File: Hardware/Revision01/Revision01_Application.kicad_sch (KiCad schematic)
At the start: 43 parts, among them J2 StrainConn, J3 StrainConn, J4 StrainConn, J5 StrainConn, J6 StrainConn, J7 StrainConn, J8 StrainConn, J9 StrainConn, Q3 NMOS, Q4 PMOS, Q6 PMOS, U11 LP5813BDRRR, U2 MRF89XAM9AT-I/RM, U4 ICM-45605, U6 INA317xxDGK

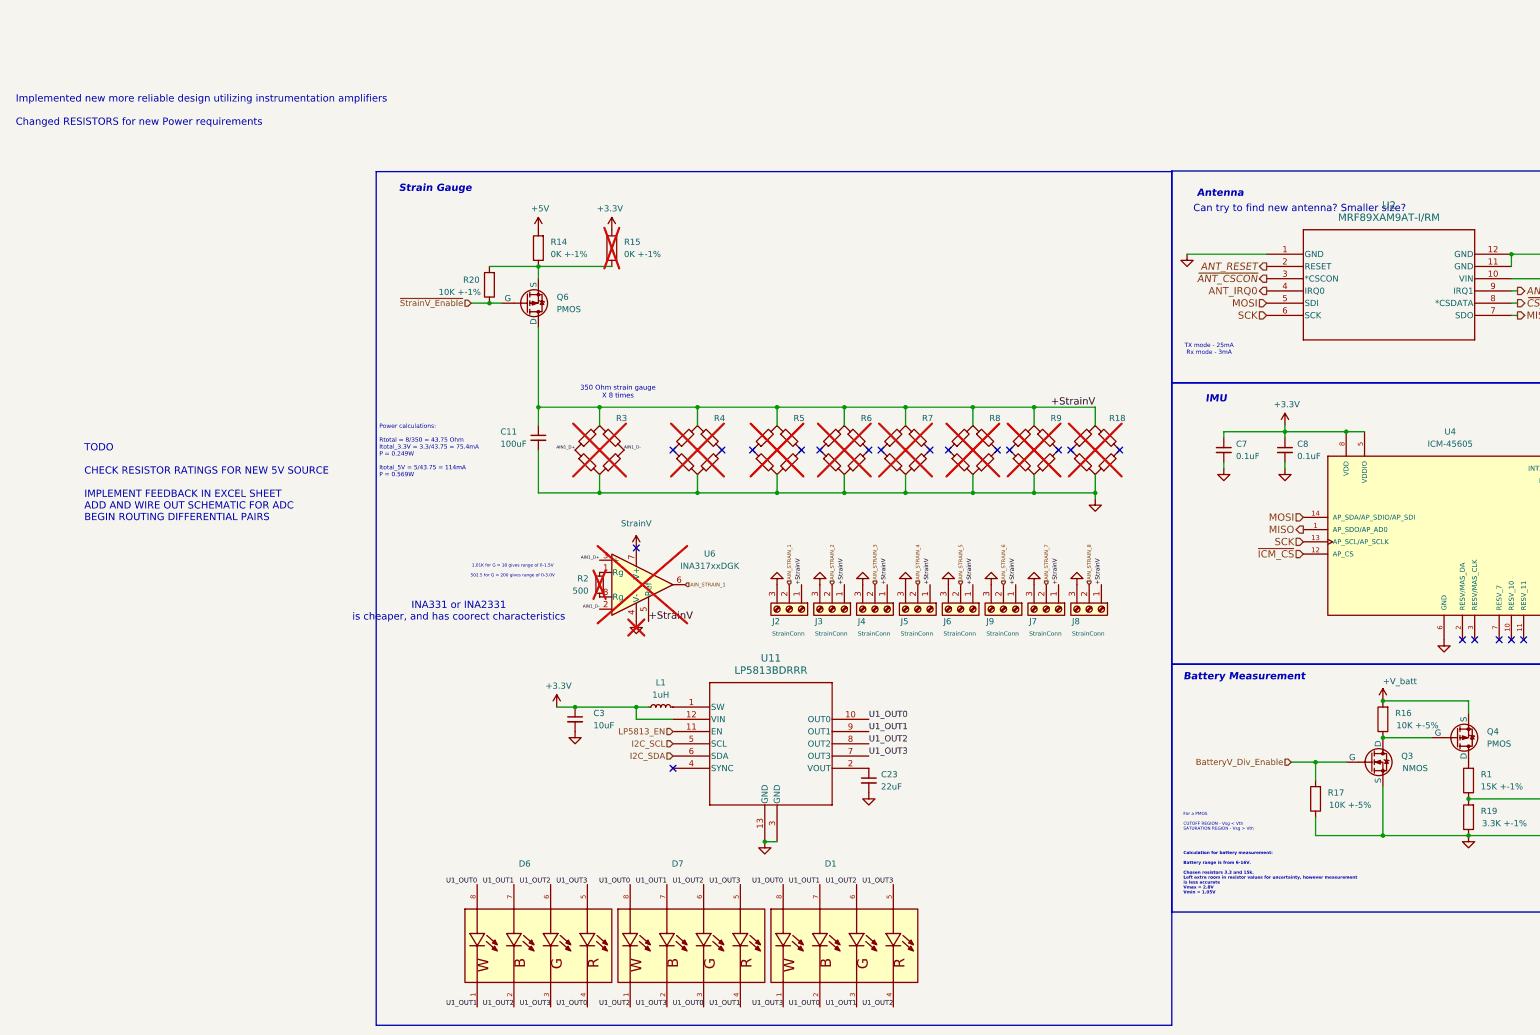
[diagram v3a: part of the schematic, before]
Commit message: Finished up small things(on schematic layout)
-Connector pins switched such that GND is pin 1
-used KICAD feature to indicate ACTIVE LOW
-polyFuse added to each StrainGauge
-Added Grounded Mounting holes connects to external GND(outside of PCB)
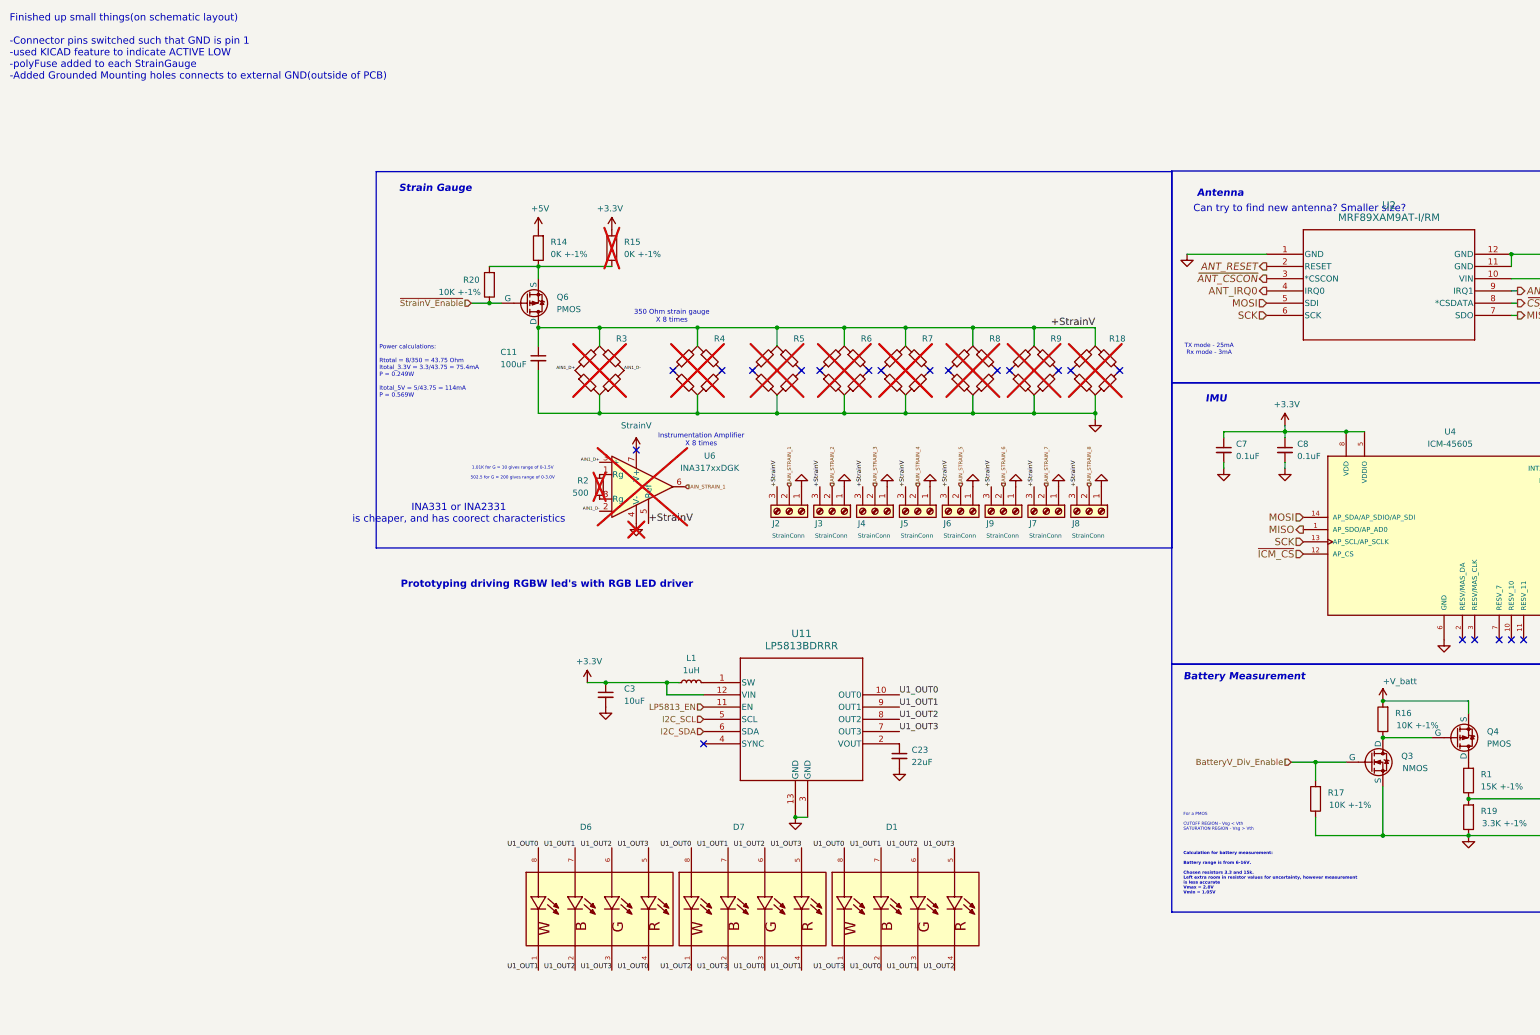
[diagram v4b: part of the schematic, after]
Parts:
- R16, R17: value 10K +-5% -> 10K +-1%
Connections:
- net +StrainV: now also J2.3 (Pin_3), J3.3 (Pin_3), J4.3 (Pin_3), J5.3 (Pin_3), J6.3 (Pin_3), J7.3 (Pin_3), J8.3 (Pin_3), J9.3 (Pin_3); no longer J2.1 (Pin_1), J3.1 (Pin_1), J4.1 (Pin_1), J5.1 (Pin_1), J6.1 (Pin_1), J7.1 (Pin_1), J8.1 (Pin_1), J9.1 (Pin_1)
- net GND: now also J2.1 (Pin_1), J3.1 (Pin_1), J4.1 (Pin_1), J5.1 (Pin_1), J6.1 (Pin_1), J7.1 (Pin_1), J8.1 (Pin_1), J9.1 (Pin_1); no longer J2.3 (Pin_3), J3.3 (Pin_3), J4.3 (Pin_3), J5.3 (Pin_3), J6.3 (Pin_3), J7.3 (Pin_3), J8.3 (Pin_3), J9.3 (Pin_3)
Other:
- note added: "Finished up small things(on schematic layout) -Connector pins switched such that GND is pin 1 -used KICAD feature to indicate ACTIVE LOW -polyFuse added to each StrainGauge -Added Grounded Mounting holes connects to external GND(outside of PCB)"
- note added: "Instrumentation Amplifier X 8 times"
- note added: "Prototyping driving RGBW led's with RGB LED driver"
- note removed: "Implemented new more reliable design utilizing instrumentation amplifiers Changed RESISTORS for new Power requirements"
- note removed: "TODO CHECK RESISTOR RATINGS FOR NEW 5V SOURCE IMPLEMENT FEEDBACK IN EXCEL SHEET ADD AND WIRE OUT SCHEMATIC FOR ADC BEGIN ROUTING DIFFERENTIAL PAIRS"
- moved on the sheet: C11, C23, C3, D1, D6, D7, J2, J3, J4, J5, J6, J7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

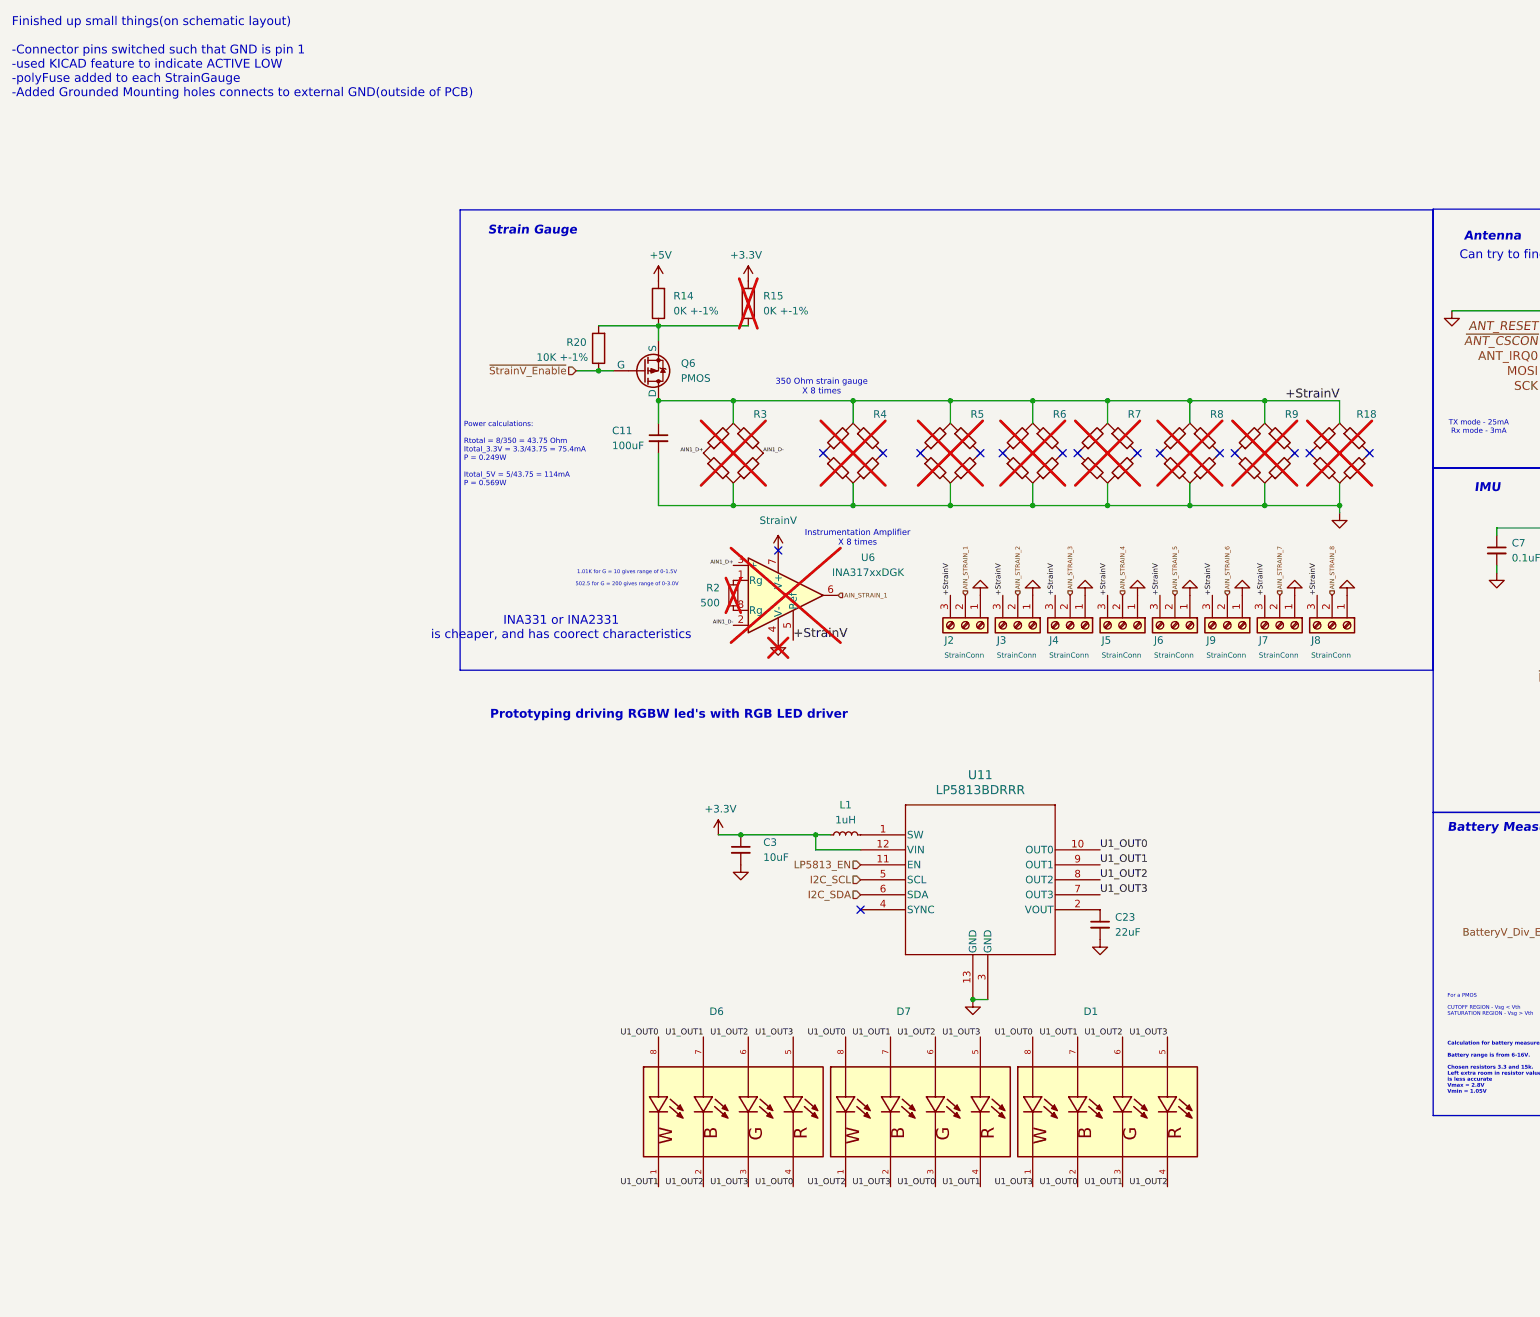
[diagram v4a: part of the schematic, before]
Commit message: I believe I have finished schematic
-Calculated RC circuit with cutoff at 10KHz for ADC
- Stimulated OP-AMP circuit with strainGauge
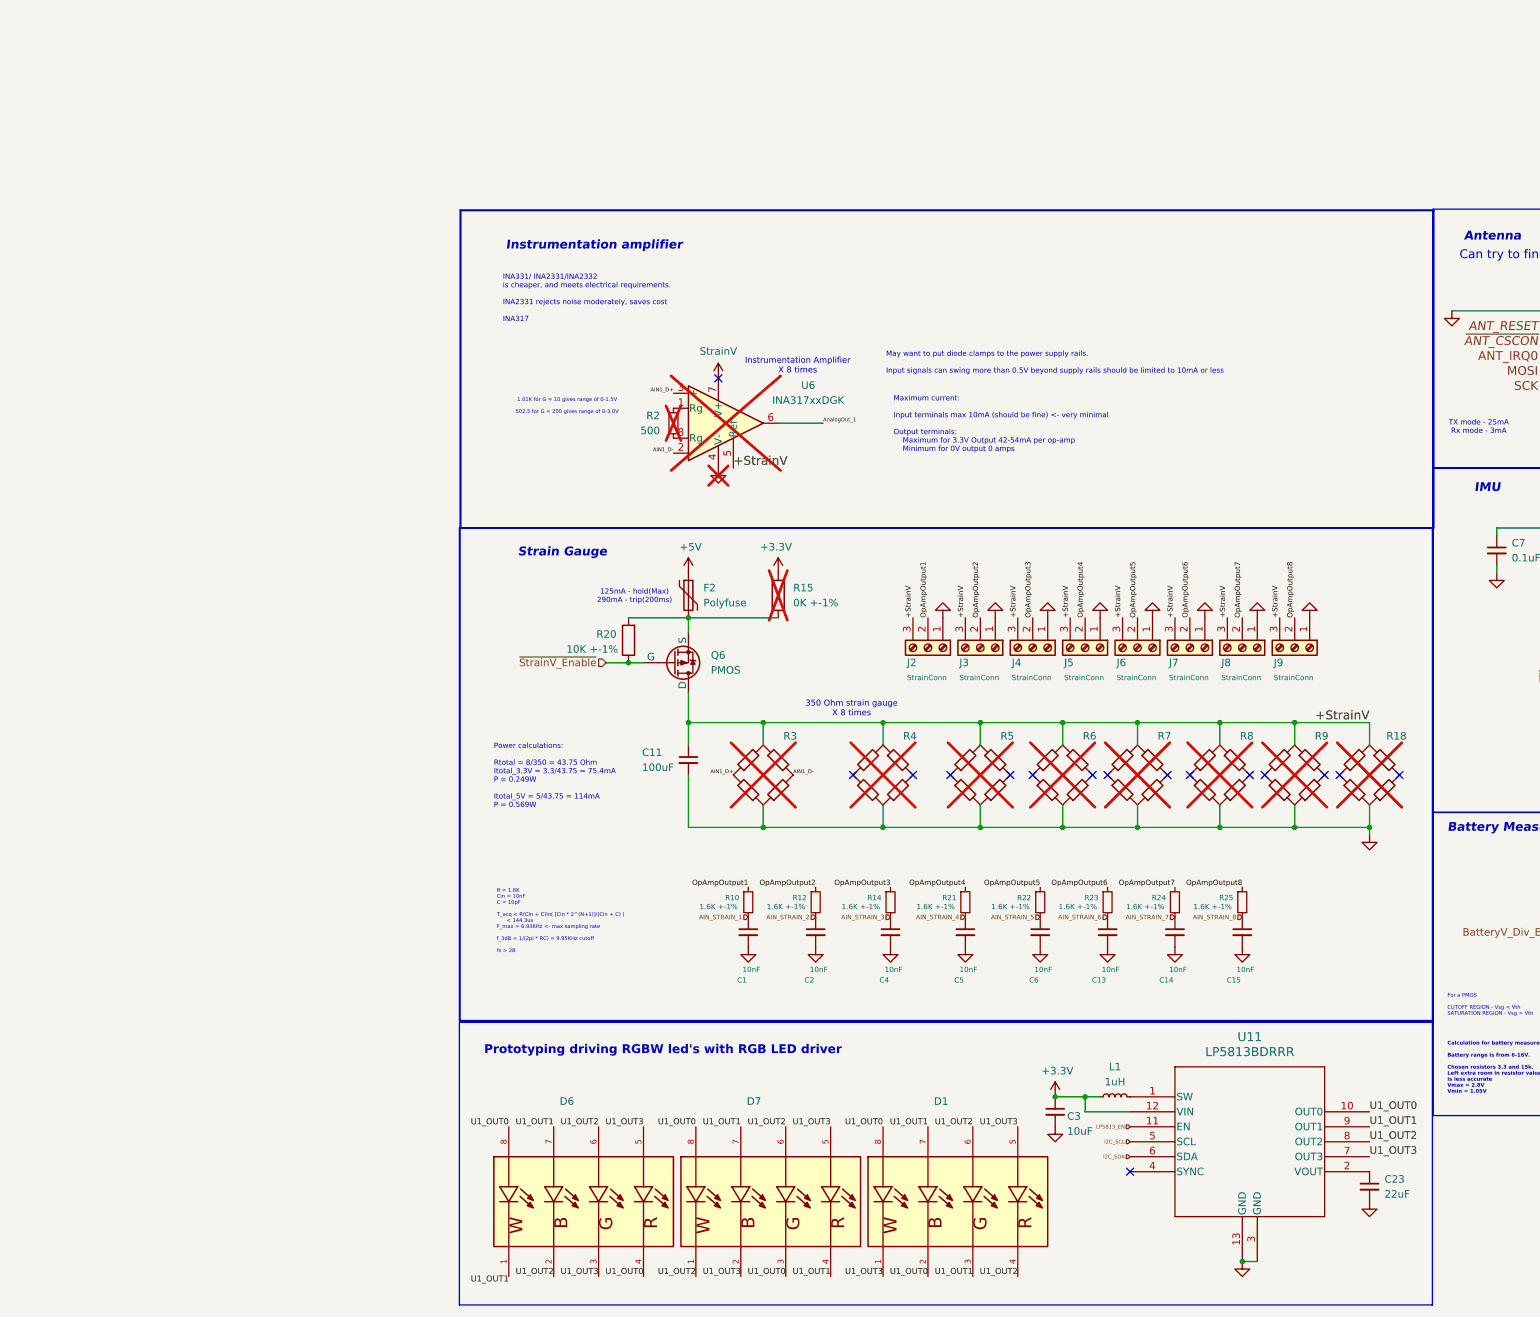
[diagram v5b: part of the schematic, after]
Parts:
- removed R14: 0K +-1%, Resistor_SMD:R_1206_3216Metric_Pad1.30x1.75mm_HandSolder, symbol Device:R
- added C1, C13, C14, C15, C2, C4, C5, C6: 10nF, Capacitor_SMD:C_0805_2012Metric_Pad1.18x1.45mm_HandSolder, symbol Device:C_Small
- added F2: Polyfuse, Resistor_SMD:R_1206_3216Metric_Pad1.30x1.75mm_HandSolder, symbol Device:Polyfuse
- added R10, R12, R14, R21, R22, R23, R24, R25: 1.6K +-1%, Resistor_SMD:R_0815_2038Metric, symbol Device:R_Small
- C23: footprint Capacitor_SMD:C_0603_1608Metric_Pad1.08x0.95mm_HandSolder -> Capacitor_SMD:C_0805_2012Metric_Pad1.18x1.45mm_HandSolder; Distributor link (none) -> https://www.digikey.ca/en/products/detail/kemet/C0805C224K5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; Manufacturer (none) -> Kemet; Manufacturer Part Number (none) -> C0805C224K5RACTU
- J2, J3, J4, J5, J6, J7, J8, J9: Distributor link (none) -> https://www.digikey.ca/en/products/detail/w-rth-elektronik/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; Manufacturer (none) -> Würth Elektronik; Manufacturer Part Number (none) -> 691137710003
- L1: footprint Inductor_SMD:L_0201_0603Metric_Pad0.64x0.40mm_HandSolder -> Inductor_SMD:L_0805_2012Metric_Pad1.15x1.40mm_HandSolder; Distributor link (none) -> https://www.digikey.ca/en/products/detail/tdk-corporation/M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; Manufacturer (none) -> TDK Corporation; Manufacturer Part Number (none) -> MLP2012S1R0MT0S1
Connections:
- net +5V: now also F2.1
- net AIN_STRAIN_1: now also C1.1, R10.2; no longer J2.2 (Pin_2), U6.6
- net AIN_STRAIN_2: now also C2.1, R12.2; no longer J3.2 (Pin_2)
- net AIN_STRAIN_3: now also C4.1, R14.2; no longer J4.2 (Pin_2)
- net AIN_STRAIN_4: now also C5.1, R21.2; no longer J5.2 (Pin_2)
- net AIN_STRAIN_5: now also C6.1, R22.2; no longer J6.2 (Pin_2)
- net AIN_STRAIN_6: now also C13.1, R23.2; no longer J9.2 (Pin_2)
- net AIN_STRAIN_7: now also C14.1, R24.2; no longer J7.2 (Pin_2)
- net AIN_STRAIN_8: now also C15.1, R25.2; no longer J8.2 (Pin_2)
- net GND: now also C1.2, C13.2, C14.2, C15.2, C2.2, C4.2, C5.2, C6.2
- net U1_OUT1: no longer D6.1
- net at Q6.3 (S), R15.1, R20.2: now also F2.2
- new net AnalogOut_1: U6.6
- new net OpAmpOutput1: J2.2 (Pin_2), R10.1
- new net OpAmpOutput2: J3.2 (Pin_2), R12.1
- new net OpAmpOutput3: J4.2 (Pin_2), R14.1
- new net OpAmpOutput4: J5.2 (Pin_2), R21.1
- new net OpAmpOutput5: J6.2 (Pin_2), R22.1
- new net OpAmpOutput6: J7.2 (Pin_2), R23.1
- new net OpAmpOutput7: J8.2 (Pin_2), R24.1
- new net OpAmpOutput8: J9.2 (Pin_2), R25.1
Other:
- note added: "125mA - hold(Max) 290mA - trip(200ms)"
- note added: "INA331/ INA2331/INA2332 is cheaper, and meets electrical requirements. INA2331 rejects noise moderately, saves cost INA317"
- note added: "Instrumentation amplifier"
- note added: "Maximum current: Input terminals max 10mA (should be fine) <- very minimal Output terminals: Maximum for 3.3V Output 42-54mA per op-amp Minimum for 0V output 0 amps"
- note added: "May want to put diode clamps to the power supply rails. Input signals can swing more than 0.5V beyond supply rails should be limited to 10mA or less"
- note added: "R = 1.6K Cin = 10nF C = 10pF T_acq < R(Cin + C)ln( [Cin * 2^(N+1)]/(Cin + C) ) < 144.3us F_max = 6.93KHz <- max sampling rate f_3dB = 1/(2pi * RC) = 9.95KHz cutoff fs > 2B"
- note removed: "Finished up small things(on schematic layout) -Connector pins switched such that GND is pin 1 -used KICAD feature to indicate ACTIVE LOW -polyFuse added to each StrainGauge -Added Grounded Mounting holes connects to external GND(outside of PCB)"
- note removed: "INA331 or INA2331 is cheaper, and has coorect characteristics"
- moved on the sheet: C11, C23, C3, D1, D6, D7, J2, J3, J4, J5, J6, J7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
